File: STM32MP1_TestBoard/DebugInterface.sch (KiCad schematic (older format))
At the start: 5 parts, among them SW2 SW_SPST, U1 STM32MP157xAB

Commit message: layout update
backup. work in progress
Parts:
- JP5: footprint (none) -> Jumper:SolderJumper-2_P1.3mm_Bridged_RoundedPad1.0x1.5mm
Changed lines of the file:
@@
 F 0 "JP5" V 9075 6125 50  0000 L CNN
 F 1 "Jumper_NC_Small" V 9120 6124 50  0001 L CNN
-F 2 "" H 9075 6050 50  0001 C CNN
+F 2 "Jumper:SolderJumper-2_P1.3mm_Bridged_RoundedPad1.0x1.5mm" H 9075 6050 50  0001 C CNN
 F 3 "~" H 9075 6050 50  0001 C CNN
 	1    9075 6050

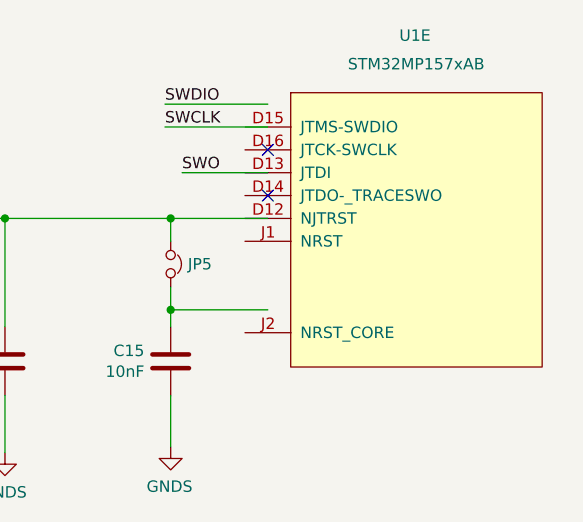
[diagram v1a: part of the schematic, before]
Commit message: updated to use stm32MP15x symbol library
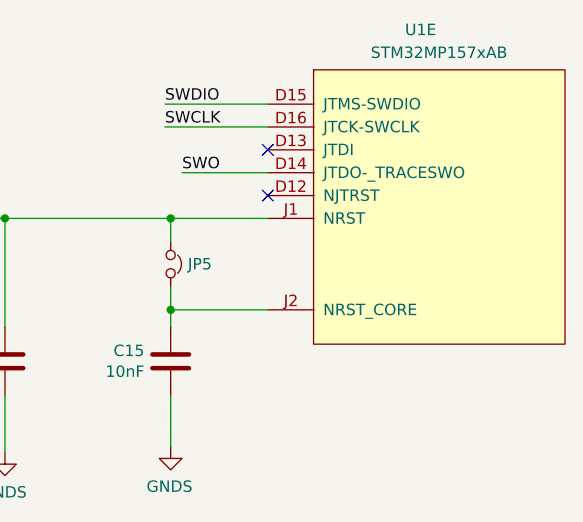
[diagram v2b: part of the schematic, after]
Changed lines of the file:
@@
 	-1   0    0    -1
-$EndComp
-$Comp
-L STM32MP15x:STM32MP157xAB U1
-U 5 1 606FB331
-P 10150 5750
-F 0 "U1" H 10075 6450 50  0000 L CNN
-F 1 "STM32MP157xAB" H 9850 6325 50  0000 L CNN
-F 2 "STM32MP151_LFBGA:BGA-361_19x19_16.0x16.0mm" H 10000 7650 50  0001 C CNN
-F 3 "https://www.st.com/resource/en/datasheet/stm32mp151c.pdf" H 10650 6150 50  0001 C CNN
-	5    10150 5750
-	1    0    0    -1
 $EndComp
 Connection ~ 8350 5850
@@
 Wire Wire Line
 	4675 5525 5200 5525
+$Comp
+L STM32MP15x:STM32MP157xAB U1
+U 5 1 5FC56421
+P 10250 5650
+F 0 "U1" H 10100 6275 50  0000 L CNN
+F 1 "STM32MP157xAB" H 9950 6175 50  0000 L CNN
+F 2 "STM32MP151_LFBGA:BGA-361_19x19_16.0x16.0mm" H 10100 7550 50  0001 C CNN
+F 3 "https://www.st.com/resource/en/datasheet/stm32mp151c.pdf" H 10900 5800 50  0001 C CNN
+	5    10250 5650
+	1    0    0    -1
+$EndComp
 $EndSCHEMATC

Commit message: updated schema and bom docs
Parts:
- U1: value STM32MP157xAB -> STM32MP157xAC
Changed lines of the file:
@@
 F 2 "Button_Switch_SMD:Panasonic_EVQPUK_EVQPUB" H 7750 6500 50  0001 C CNN
 F 3 "https://industrial.panasonic.com/cdbs/www-data/pdf/ATK0000/ATK0000C382.pdf" H 7750 6500 50  0001 C CNN
+F 4 "~" H 7750 6500 50  0001 C CNN "Mfr"
+F 5 "~" H 7750 6500 50  0001 C CNN "PartNo"
 	1    7750 6500
 	0    -1   1    0
@@
 F 2 "Jumper:SolderJumper-2_P1.3mm_Bridged_RoundedPad1.0x1.5mm" H 9075 6050 50  0001 C CNN
 F 3 "~" H 9075 6050 50  0001 C CNN
+F 4 "~" H 9075 6050 50  0001 C CNN "Mfr"
+F 5 "~" H 9075 6050 50  0001 C CNN "PartNo"
 	1    9075 6050
 	0    1    1    0
@@
 P 10250 5650
 F 0 "U1" H 10100 6275 50  0000 L CNN
-F 1 "STM32MP157xAB" H 9950 6175 50  0000 L CNN
+F 1 "STM32MP157xAC" H 9950 6175 50  0000 L CNN
 F 2 "STM32MP151_LFBGA:BGA-361_19x19_16.0x16.0mm" H 10100 7550 50  0001 C CNN
 F 3 "https://www.st.com/resource/en/datasheet/stm32mp151c.pdf" H 10900 5800 50  0001 C CNN
+F 4 "~" H 10250 5650 50  0001 C CNN "Mfr"
+F 5 "~" H 10250 5650 50  0001 C CNN "PartNo"
 	5    10250 5650
 	1    0    0    -1

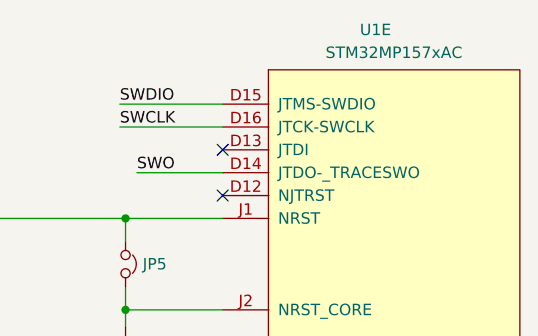
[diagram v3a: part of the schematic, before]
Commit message: corrected STM32MP157 footprint
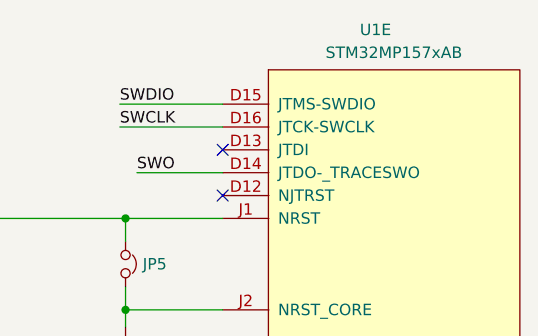
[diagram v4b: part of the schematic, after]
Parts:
- U1: value STM32MP157xAC -> STM32MP157xAB; footprint STM32MP151_LFBGA:BGA-361_19x19_16.0x16.0mm -> STM32MP151_LFBGA:BGA-354_19x19_16.0x16.0mm
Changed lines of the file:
@@
 P 10250 5650
 F 0 "U1" H 10100 6275 50  0000 L CNN
-F 1 "STM32MP157xAC" H 9950 6175 50  0000 L CNN
-F 2 "STM32MP151_LFBGA:BGA-361_19x19_16.0x16.0mm" H 10100 7550 50  0001 C CNN
+F 1 "STM32MP157xAB" H 9950 6175 50  0000 L CNN
+F 2 "STM32MP151_LFBGA:BGA-354_19x19_16.0x16.0mm" H 10100 7550 50  0001 C CNN
 F 3 "https://www.st.com/resource/en/datasheet/stm32mp151c.pdf" H 10900 5800 50  0001 C CNN
 F 4 "~" H 10250 5650 50  0001 C CNN "Mfr"
